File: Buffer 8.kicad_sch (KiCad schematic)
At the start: 2 parts, among them U1407 74HC245

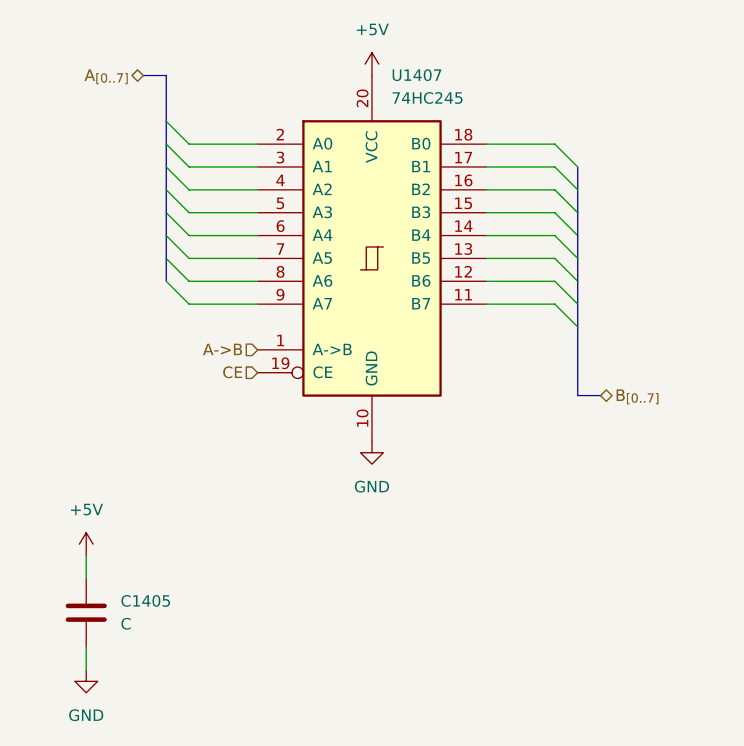
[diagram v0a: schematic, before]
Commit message: More cleanup and preparing signals for control logic
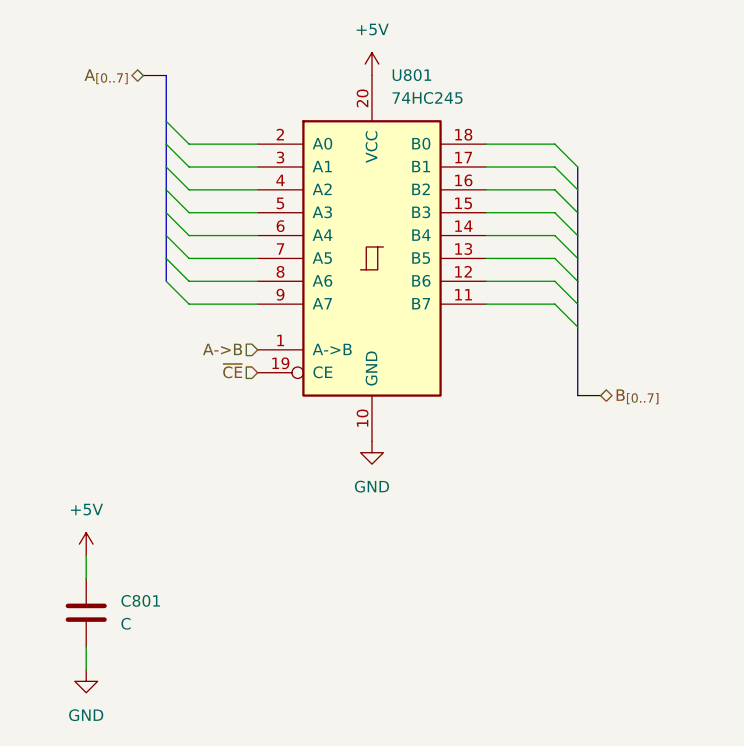
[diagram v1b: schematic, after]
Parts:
- renumbered C1405 to C801, U1407 to U801
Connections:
- net CE renamed ~{CE}
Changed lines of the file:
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@@
 		)
 	)
-	(hierarchical_label "CE"
+	(hierarchical_label "~{CE}"
 		(shape input)
 		(at 100.33 90.17 180)
@@
 		(dnp no)
 		(fields_autoplaced yes)
-		(property "Reference" "#PWR01414"
+		(property "Reference" "#PWR0802"
 			(at 81.28 129.54 0)
 			(effects
@@
 			(project "BRISC8"
 				(path "/e198223b-f7bd-4b26-ae2e-259db8d07fb6/d081cdcb-1181-4657-9580-dc3ba9a85775/91ebbdfa-d43d-4c9d-8ef6-4e72d6db27fd"
-					(reference "#PWR01414")
+					(reference "#PWR0802")
 					(unit 1)
 				)
@@
 		(dnp no)
 		(fields_autoplaced yes)
-		(property "Reference" "#PWR01411"
+		(property "Reference" "#PWR0803"
 			(at 113.03 60.96 0)
 			(effects
@@
 			(project "BRISC8"
 				(path "/e198223b-f7bd-4b26-ae2e-259db8d07fb6/d081cdcb-1181-4657-9580-dc3ba9a85775/91ebbdfa-d43d-4c9d-8ef6-4e72d6db27fd"
-					(reference "#PWR01411")
+					(reference "#PWR0803")
 					(unit 1)
 				)
@@
 		(dnp no)
 		(fields_autoplaced yes)
-		(property "Reference" "#PWR01412"
+		(property "Reference" "#PWR0804"
 			(at 113.03 104.14 0)
 			(effects
@@
 			(project "BRISC8"
 				(path "/e198223b-f7bd-4b26-ae2e-259db8d07fb6/d081cdcb-1181-4657-9580-dc3ba9a85775/91ebbdfa-d43d-4c9d-8ef6-4e72d6db27fd"
-					(reference "#PWR01412")
+					(reference "#PWR0804")
 					(unit 1)
 				)
@@
 		(dnp no)
 		(fields_autoplaced yes)
-		(property "Reference" "#PWR01413"
+		(property "Reference" "#PWR0801"
 			(at 81.28 114.3 0)
 			(effects
@@
 			(project "BRISC8"
 				(path "/e198223b-f7bd-4b26-ae2e-259db8d07fb6/d081cdcb-1181-4657-9580-dc3ba9a85775/91ebbdfa-d43d-4c9d-8ef6-4e72d6db27fd"
-					(reference "#PWR01413")
+					(reference "#PWR0801")
 					(unit 1)
 				)
@@
 		(dnp no)
 		(fields_autoplaced yes)
-		(property "Reference" "U1407"
+		(property "Reference" "U801"
 			(at 115.1733 57.15 0)
 			(effects
@@
 			(project "BRISC8"
 				(path "/e198223b-f7bd-4b26-ae2e-259db8d07fb6/d081cdcb-1181-4657-9580-dc3ba9a85775/91ebbdfa-d43d-4c9d-8ef6-4e72d6db27fd"
-					(reference "U1407")
+					(reference "U801")
 					(unit 1)
 				)
@@
 		(dnp no)
 		(fields_autoplaced yes)
-		(property "Reference" "C1405"
+		(property "Reference" "C801"
 			(at 85.09 115.5699 0)
 			(effects
@@
 			(project "BRISC8"
 				(path "/e198223b-f7bd-4b26-ae2e-259db8d07fb6/d081cdcb-1181-4657-9580-dc3ba9a85775/91ebbdfa-d43d-4c9d-8ef6-4e72d6db27fd"
-					(reference "C1405")
-					(unit 1)
-				)
+					(reference "C801")
+					(unit 1)
+				)

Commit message: Draft Schematic
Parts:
- C801: value C -> 0.1uF; footprint (none) -> Capacitor_THT:C_Rect_L4.0mm_W2.5mm_P2.50mm
- U801: footprint (none) -> Package_DIP:DIP-20_W7.62mm
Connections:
- net B_{7}: now reaches U801.11 (B7)
- net B_{6}: now reaches U801.12 (B6)
- net B_{5}: now reaches U801.13 (B5)
- net B_{4}: now reaches U801.14 (B4)
- net B_{3}: now reaches U801.15 (B3)
- net B_{2}: now reaches U801.16 (B2)
- net B_{1}: now reaches U801.17 (B1)
- net B_{0}: now reaches U801.18 (B0)
- net A_{0}: now reaches U801.2 (A0)
- net A_{1}: now reaches U801.3 (A1)
- net A_{2}: now reaches U801.4 (A2)
- net A_{3}: now reaches U801.5 (A3)
- net A_{4}: now reaches U801.6 (A4)
- net A_{5}: now reaches U801.7 (A5)
- net A_{6}: now reaches U801.8 (A6)
- net A_{7}: now reaches U801.9 (A7)
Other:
- company: (none) -> Brian Duffy
- title: (none) -> BRISC8 CPU
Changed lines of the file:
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@@
 	(generator "eeschema")
 	(generator_version "9.0")
-	(paper "A4")
+	(paper "USLetter")
+	(title_block
+		(title "BRISC8 CPU")
+		(date "2025-06-26")
+		(rev "v1.0.0")
+		(company "Brian Duffy")
+		(comment 3 "Compatible with the BRISC8 assembler and compiler suite.")
+		(comment 4 "Simple 8-bit RISC CPU designed by Brian Duffy to explore the lowest level of computing.")
+	)
 	(bus_entry
 		(at 133.35 67.31)
@@
 			(width 0)
 			(type default)
+		)
+	)
+	(label "B_{7}"
+		(at 133.35 82.55 180)
+		(effects
+			(font
+				(size 1.27 1.27)
+			)
+			(justify right bottom)
+		)
+	)
+	(label "A_{4}"
+		(at 92.71 74.93 0)
+		(effects
+			(font
+				(size 1.27 1.27)
+			)
+			(justify left bottom)
+		)
+	)
+	(label "B_{4}"
+		(at 133.35 74.93 180)
+		(effects
+			(font
+				(size 1.27 1.27)
+			)
+			(justify right bottom)
+		)
+	)
+	(label "A_{1}"
+		(at 92.71 67.31 0)
+		(effects
+			(font
+				(size 1.27 1.27)
+			)
+			(justify left bottom)
+		)
+	)
+	(label "A_{0}"
+		(at 92.71 64.77 0)
+		(effects
+			(font
+				(size 1.27 1.27)
+			)
+			(justify left bottom)
+		)
+	)
+	(label "B_{6}"
+		(at 133.35 80.01 180)
+		(effects
+			(font
+				(size 1.27 1.27)
+			)
+			(justify right bottom)
+		)
+	)
+	(label "A_{5}"
+		(at 92.71 77.47 0)
+		(effects
+			(font
+				(size 1.27 1.27)
+			)
+			(justify left bottom)
+		)
+	)
+	(label "B_{0}"
+		(at 133.35 64.77 180)
+		(effects
+			(font
+				(size 1.27 1.27)
+			)
+			(justify right bottom)
+		)
+	)
+	(label "A_{2}"
+		(at 92.71 69.85 0)
+		(effects
+			(font
+				(size 1.27 1.27)
+			)
+			(justify left bottom)
+		)
+	)
+	(label "B_{3}"
+		(at 133.35 72.39 180)
+		(effects
+			(font
+				(size 1.27 1.27)
+			)
+			(justify right bottom)
+		)
+	)
+	(label "A_{7}"
+		(at 92.71 82.55 0)
+		(effects
+			(font
+				(size 1.27 1.27)
+			)
+			(justify left bottom)
+		)
+	)
+	(label "B_{1}"
+		(at 133.35 67.31 180)
+		(effects
+			(font
+				(size 1.27 1.27)
+			)
+			(justify right bottom)
+		)
+	)
+	(label "B_{2}"
+		(at 133.35 69.85 180)
+		(effects
+			(font
+				(size 1.27 1.27)
+			)
+			(justify right bottom)
+		)
+	)
+	(label "B_{5}"
+		(at 133.35 77.47 180)
+		(effects
+			(font
+				(size 1.27 1.27)
+			)
+			(justify right bottom)
+		)
+	)
+	(label "A_{3}"
+		(at 92.71 72.39 0)
+		(effects
+			(font
+				(size 1.27 1.27)
+			)
+			(justify left bottom)
+		)
+	)
+	(label "A_{6}"
+		(at 92.71 80.01 0)
+		(effects
+			(font
+				(size 1.27 1.27)
+			)
+			(justify left bottom)
 		)
 	)
@@
 		(dnp no)
 		(fields_autoplaced yes)
-		(property "Reference" "#PWR0802"
+		(property "Reference" "#PWR0804"
 			(at 81.28 129.54 0)
 			(effects
@@
 			(project "BRISC8"
 				(path "/e198223b-f7bd-4b26-ae2e-259db8d07fb6/d081cdcb-1181-4657-9580-dc3ba9a85775/91ebbdfa-d43d-4c9d-8ef6-4e72d6db27fd"
-					(reference "#PWR0802")
+					(reference "#PWR0804")
 					(unit 1)
 				)
@@
 		(dnp no)
 		(fields_autoplaced yes)
-		(property "Reference" "#PWR0803"
+		(property "Reference" "#PWR0801"
 			(at 113.03 60.96 0)
 			(effects
@@
 			(project "BRISC8"
 				(path "/e198223b-f7bd-4b26-ae2e-259db8d07fb6/d081cdcb-1181-4657-9580-dc3ba9a85775/91ebbdfa-d43d-4c9d-8ef6-4e72d6db27fd"
-					(reference "#PWR0803")
+					(reference "#PWR0801")
 					(unit 1)
 				)
@@
 		(dnp no)
 		(fields_autoplaced yes)
-		(property "Reference" "#PWR0804"
+		(property "Reference" "#PWR0802"
 			(at 113.03 104.14 0)
 			(effects
@@
 			(project "BRISC8"
 				(path "/e198223b-f7bd-4b26-ae2e-259db8d07fb6/d081cdcb-1181-4657-9580-dc3ba9a85775/91ebbdfa-d43d-4c9d-8ef6-4e72d6db27fd"
-					(reference "#PWR0804")
+					(reference "#PWR0802")
 					(unit 1)
 				)
@@
 		(dnp no)
 		(fields_autoplaced yes)
-		(property "Reference" "#PWR0801"
+		(property "Reference" "#PWR0803"
 			(at 81.28 114.3 0)
 			(effects
@@
 			(project "BRISC8"
 				(path "/e198223b-f7bd-4b26-ae2e-259db8d07fb6/d081cdcb-1181-4657-9580-dc3ba9a85775/91ebbdfa-d43d-4c9d-8ef6-4e72d6db27fd"
-					(reference "#PWR0801")
+					(reference "#PWR0803")
 					(unit 1)
 				)
@@
 			)
 		)
-		(property "Footprint" ""
+		(property "Footprint" "Package_DIP:DIP-20_W7.62mm"
 			(at 113.03 77.47 0)
 			(effects
@@
 			)
 		)
-		(property "Value" "C"
+		(property "Value" "0.1uF"
 			(at 85.09 118.1099 0)
 			(effects
@@
 			)
 		)
-		(property "Footprint" ""
+		(property "Footprint" "Capacitor_THT:C_Rect_L4.0mm_W2.5mm_P2.50mm"
 			(at 82.2452 120.65 0)
 			(effects
